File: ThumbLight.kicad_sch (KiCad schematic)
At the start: 4 parts, among them J1 USB_A, U2 UA78M33_TO252, U3 ESP-12E, U4 TTL

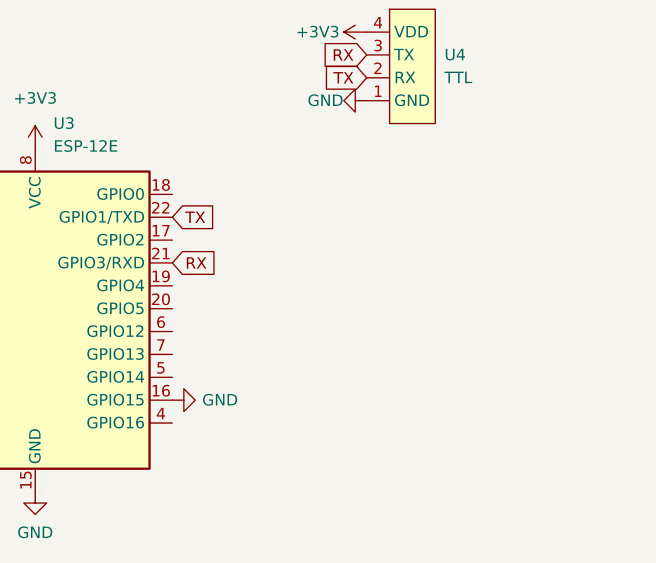
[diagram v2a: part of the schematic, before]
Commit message: Add PROGRAM Jumper as well as a DHT11 sensor
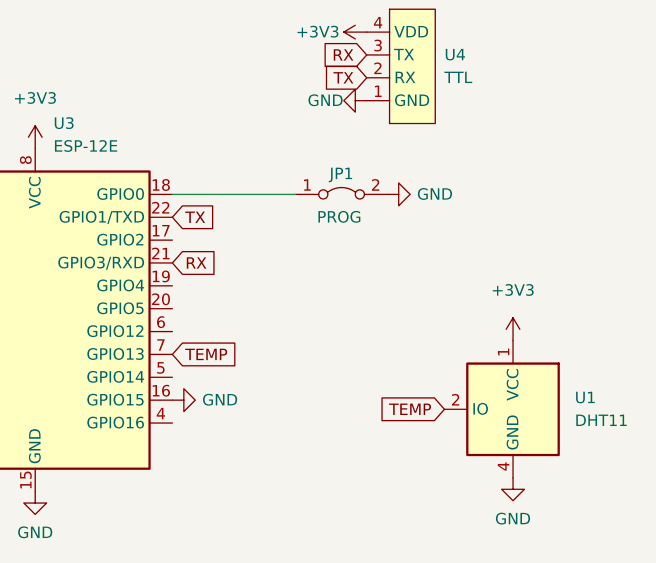
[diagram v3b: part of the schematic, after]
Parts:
- added JP1: PROG, Connector_PinHeader_2.54mm:PinHeader_1x02_P2.54mm_Vertical, symbol Jumper:Jumper_2_Bridged
- added U1: DHT11, Sensor:Aosong_DHT11_5.5x12.0_P2.54mm, symbol Sensor:DHT11
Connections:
- net +3V3: now also U1.1 (VCC)
- net GND: now also JP1.2 (B), U1.4 (GND)
- net at U3.18 (GPIO0): now also JP1.1 (A)
- net TEMP: now reaches U3.7 (GPIO13)
- net TEMP: now also U1.2 (IO)
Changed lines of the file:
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@@
   (no_connect (at 60.452 48.768))
   (no_connect (at 70.612 41.148))
+  (wire (pts (xy 141.224 48.514) (xy 154.94 48.514))
+    (stroke (width 0) (type default) (color 0 0 0 0))
+  )
   (global_label "TX" (shape input) (at 141.224 51.054 0) (fields_autoplaced)
     (effects (font (size 1.27 1.27)) (justify left))
@@
     )
   )
+  (global_label "TEMP" (shape input) (at 171.45 72.39 180) (fields_autoplaced)
+    (effects (font (size 1.27 1.27)) (justify right))
+    (property "Intersheet References" "${INTERSHEET_REFS}" (id 0) (at 164.1988 72.3106 0)
+      (effects (font (size 1.27 1.27)) (justify right) hide)
+    )
+  )
   (global_label "RX" (shape input) (at 141.224 56.134 0) (fields_autoplaced)
     (effects (font (size 1.27 1.27)) (justify left))
@@
     )
   )
+  (global_label "TEMP" (shape input) (at 141.224 66.294 0) (fields_autoplaced)
+    (effects (font (size 1.27 1.27)) (justify left))
+    (property "Intersheet References" "${INTERSHEET_REFS}" (id 0) (at 148.4752 66.3734 0)
+      (effects (font (size 1.27 1.27)) (justify left) hide)
+    )
+  )
+  (symbol (lib_id "power:+3V3") (at 179.07 64.77 0) (mirror y) (unit 1)
+    (in_bom yes) (on_board yes) (fields_autoplaced)
+    (property "Reference" "#PWR0114" (id 0) (at 179.07 68.58 0)
+      (effects (font (size 1.27 1.27)) hide)
+    )
+    (property "Value" "+3V3" (id 1) (at 179.07 59.182 0))
+    (property "Footprint" "" (id 2) (at 179.07 64.77 0)
+      (effects (font (size 1.27 1.27)) hide)
+    )
+    (property "Datasheet" "" (id 3) (at 179.07 64.77 0)
+      (effects (font (size 1.27 1.27)) hide)
+    )
+    (pin "1")
+  )
   (symbol (lib_id "power:GND") (at 141.224 71.374 90) (unit 1)
     (in_bom yes) (on_board yes) (fields_autoplaced)
@@
     )
     (pin "1")
+  )
+  (symbol (lib_id "Sensor:DHT11") (at 179.07 72.39 0) (mirror y) (unit 1)
+    (in_bom yes) (on_board yes) (fields_autoplaced)
+    (property "Reference" "U1" (id 0) (at 185.928 71.1199 0)
+      (effects (font (size 1.27 1.27)) (justify right))
+    )
+    (property "Value" "DHT11" (id 1) (at 185.928 73.6599 0)
+      (effects (font (size 1.27 1.27)) (justify right))
+    )
+    (property "Footprint" "Sensor:Aosong_DHT11_5.5x12.0_P2.54mm" (id 2) (at 179.07 82.55 0)
+      (effects (font (size 1.27 1.27)) hide)
+    )
+    (property "Datasheet" "http://akizukidenshi.com/download/ds/aosong/DHT11.pdf" (id 3) (at 175.26 66.04 0)
+      (effects (font (size 1.27 1.27)) hide)
+    )
+    (pin "1")
+    (pin "2")
+    (pin "3")
+    (pin "4")
   )
   (symbol (lib_id "power:+3V3") (at 162.814 30.48 90) (unit 1)
@@
     (pin "9")
   )
+  (symbol (lib_id "Jumper:Jumper_2_Bridged") (at 160.02 48.514 0) (unit 1)
+    (in_bom yes) (on_board yes)
+    (property "Reference" "JP1" (id 0) (at 160.02 46.228 0))
+    (property "Value" "PROG" (id 1) (at 159.766 51.054 0))
+    (property "Footprint" "Connector_PinHeader_2.54mm:PinHeader_1x02_P2.54mm_Vertical" (id 2) (at 160.02 48.514 0)
+      (effects (font (size 1.27 1.27)) hide)
+    )
+    (property "Datasheet" "~" (id 3) (at 160.02 48.514 0)
+      (effects (font (size 1.27 1.27)) hide)
+    )
+    (pin "1")
+    (pin "2")
+  )
   (symbol (lib_id "power:+3V3") (at 110.744 53.594 90) (unit 1)
     (in_bom yes) (on_board yes)
@@
     )
     (property "Datasheet" "" (id 3) (at 162.814 38.1 0)
+      (effects (font (size 1.27 1.27)) hide)
+    )
+    (pin "1")
+  )
+  (symbol (lib_id "power:GND") (at 179.07 80.01 0) (mirror y) (unit 1)
+    (in_bom yes) (on_board yes) (fields_autoplaced)
+    (property "Reference" "#PWR0113" (id 0) (at 179.07 86.36 0)
+      (effects (font (size 1.27 1.27)) hide)
+    )
+    (property "Value" "GND" (id 1) (at 179.07 84.582 0))
+    (property "Footprint" "" (id 2) (at 179.07 80.01 0)
+      (effects (font (size 1.27 1.27)) hide)
+    )
+    (property "Datasheet" "" (id 3) (at 179.07 80.01 0)
+      (effects (font (size 1.27 1.27)) hide)
+    )
+    (pin "1")
+  )
+  (symbol (lib_id "power:GND") (at 165.1 48.514 90) (unit 1)
+    (in_bom yes) (on_board yes) (fields_autoplaced)
+    (property "Reference" "#PWR0112" (id 0) (at 171.45 48.514 0)
+      (effects (font (size 1.27 1.27)) hide)
+    )
+    (property "Value" "GND" (id 1) (at 168.402 48.5139 90)
+      (effects (font (size 1.27 1.27)) (justify right))
+    )
+    (property "Footprint" "" (id 2) (at 165.1 48.514 0)
+      (effects (font (size 1.27 1.27)) hide)
+    )
+    (property "Datasheet" "" (id 3) (at 165.1 48.514 0)
       (effects (font (size 1.27 1.27)) hide)
     )
@@
       (reference "#PWR0111") (unit 1) (value "GND") (footprint "")
     )
+    (path "/cecaeb11-c18e-436a-b913-ea98641a8577"
+      (reference "#PWR0112") (unit 1) (value "GND") (footprint "")
+    )
+    (path "/cd1319fe-9fb0-446c-90b1-41f07d211857"
+      (reference "#PWR0113") (unit 1) (value "GND") (footprint "")
+    )
+    (path "/1537578c-25a2-4583-94d3-02f62cf698e2"
+      (reference "#PWR0114") (unit 1) (value "+3V3") (footprint "")
+    )
     (path "/b11863f2-05f0-4c70-9612-53388c5c7348"
       (reference "J1") (unit 1) (value "USB_A") (footprint "Connector_USB:USB_A_CNCTech_1001-011-01101_Horizontal")
     )
+    (path "/8fe39038-0f26-46f1-8a00-7161b7c20514"
+      (reference "JP1") (unit 1) (value "PROG") (footprint "Connector_PinHeader_2.54mm:PinHeader_1x02_P2.54mm_Vertical")
+    )
+    (path "/48072e63-67ef-42f2-9dd9-98f22a40c240"
+      (reference "U1") (unit 1) (value "DHT11") (footprint "Sensor:Aosong_DHT11_5.5x12.0_P2.54mm")
+    )
     (path "/efad0331-27eb-4636-86a4-200955527a64"

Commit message: Add USB Footprint
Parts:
- J1: footprint Connector_USB:USB_A_CNCTech_1001-011-01101_Horizontal -> usb-a-pcb:usb-a-pcb
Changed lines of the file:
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@@
     (property "Reference" "J1" (id 0) (at 62.992 25.4 0))
     (property "Value" "USB_A" (id 1) (at 62.992 27.94 0))
-    (property "Footprint" "Connector_USB:USB_A_CNCTech_1001-011-01101_Horizontal" (id 2) (at 66.802 39.878 0)
+    (property "Footprint" "usb-a-pcb:usb-a-pcb" (id 2) (at 66.802 39.878 0)
       (effects (font (size 1.27 1.27)) hide)
     )
@@
     )
     (path "/b11863f2-05f0-4c70-9612-53388c5c7348"
-      (reference "J1") (unit 1) (value "USB_A") (footprint "Connector_USB:USB_A_CNCTech_1001-011-01101_Horizontal")
+      (reference "J1") (unit 1) (value "USB_A") (footprint "usb-a-pcb:usb-a-pcb")
     )
     (path "/8fe39038-0f26-46f1-8a00-7161b7c20514"

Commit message: New basic layout
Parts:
- JP1: footprint Connector_PinHeader_2.54mm:PinHeader_1x02_P2.54mm_Vertical -> Connector_PinHeader_2.54mm:PinHeader_1x03_P2.54mm_Vertical
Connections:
- net TEMP: now also U3.19 (GPIO4); no longer U3.7 (GPIO13)
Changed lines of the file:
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@@
     )
   )
-  (global_label "TEMP" (shape input) (at 141.224 66.294 0) (fields_autoplaced)
+  (global_label "TEMP" (shape input) (at 141.224 58.674 0) (fields_autoplaced)
     (effects (font (size 1.27 1.27)) (justify left))
-    (property "Intersheet References" "${INTERSHEET_REFS}" (id 0) (at 148.4752 66.3734 0)
+    (property "Intersheet References" "${INTERSHEET_REFS}" (id 0) (at 148.4752 58.7534 0)
       (effects (font (size 1.27 1.27)) (justify left) hide)
     )
@@
     (property "Reference" "JP1" (id 0) (at 160.02 46.228 0))
     (property "Value" "PROG" (id 1) (at 159.766 51.054 0))
-    (property "Footprint" "Connector_PinHeader_2.54mm:PinHeader_1x02_P2.54mm_Vertical" (id 2) (at 160.02 48.514 0)
+    (property "Footprint" "Connector_PinHeader_2.54mm:PinHeader_1x03_P2.54mm_Vertical" (id 2) (at 160.02 48.514 0)
       (effects (font (size 1.27 1.27)) hide)
     )
@@
     )
     (path "/8fe39038-0f26-46f1-8a00-7161b7c20514"
-      (reference "JP1") (unit 1) (value "PROG") (footprint "Connector_PinHeader_2.54mm:PinHeader_1x02_P2.54mm_Vertical")
+      (reference "JP1") (unit 1) (value "PROG") (footprint "Connector_PinHeader_2.54mm:PinHeader_1x03_P2.54mm_Vertical")
     )
     (path "/48072e63-67ef-42f2-9dd9-98f22a40c240"

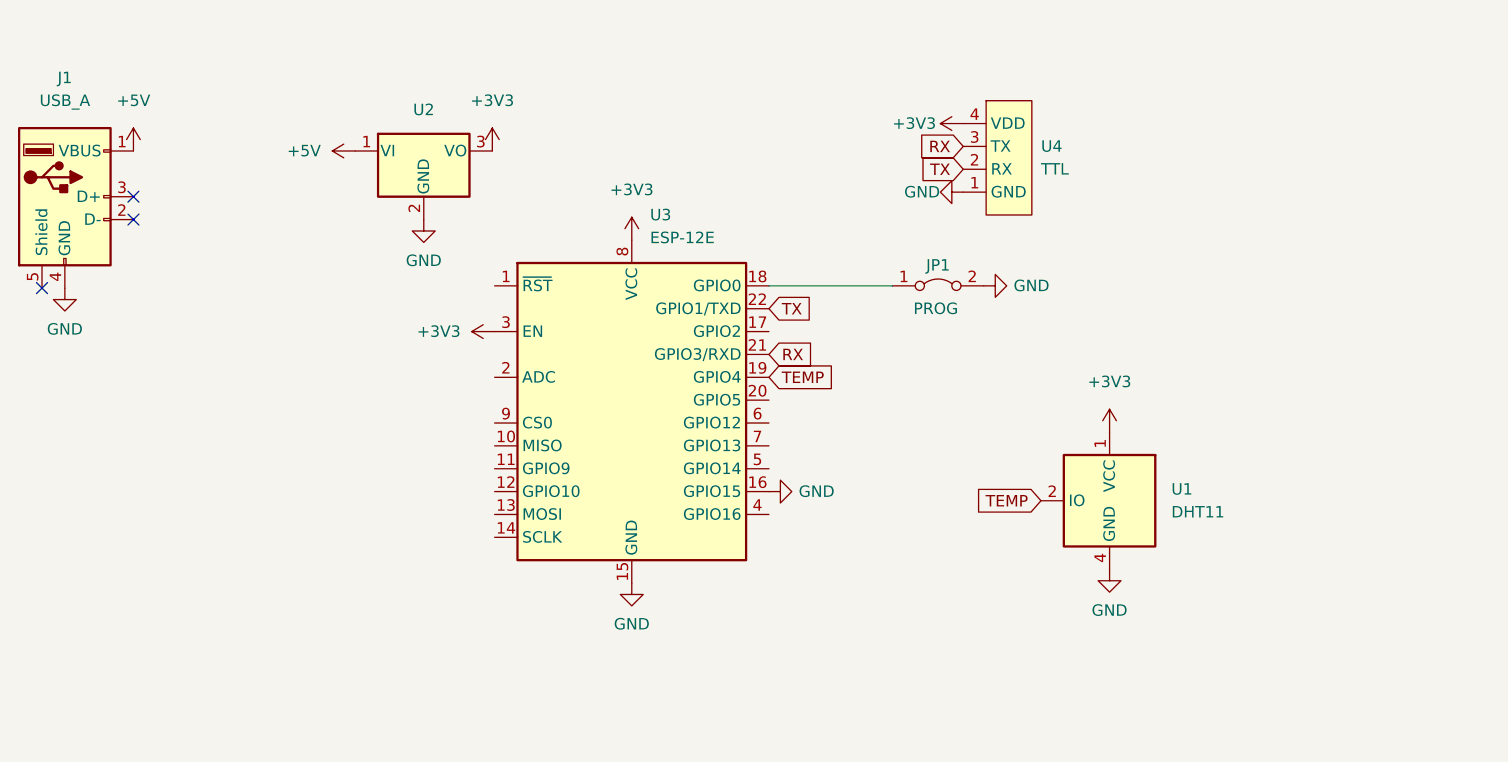
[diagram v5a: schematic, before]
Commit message: Add neopixel strip
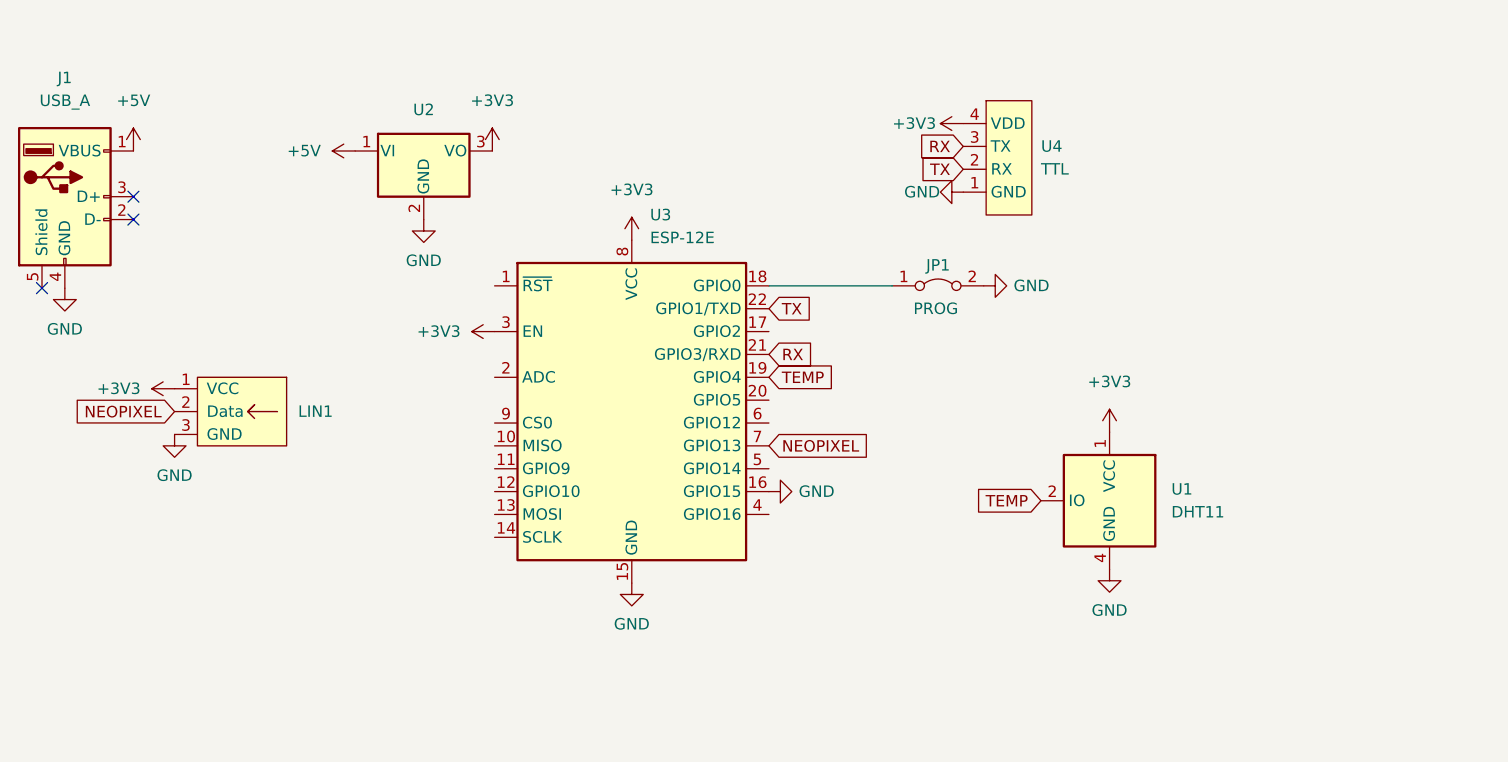
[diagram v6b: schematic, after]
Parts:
- added LIN1: LEDs_In, neopixel-strip:neopixel-strip, symbol neopixel-strip:LEDs_In
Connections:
- net +3V3: now also LIN1.1 (VCC)
- net GND: now also LIN1.3 (GND)
- net NEOPIXEL: now reaches U3.7 (GPIO13)
- net NEOPIXEL: now also LIN1.2 (Data)
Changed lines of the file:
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@@
     (stroke (width 0) (type default) (color 0 0 0 0))
+  )
+  (global_label "NEOPIXEL" (shape input) (at 141.224 66.294 0) (fields_autoplaced)
+    (effects (font (size 1.27 1.27)) (justify left))
+    (property "Intersheet References" "${INTERSHEET_REFS}" (id 0) (at 152.7085 66.2146 0)
+      (effects (font (size 1.27 1.27)) (justify left) hide)
+    )
   )
   (global_label "TX" (shape input) (at 141.224 51.054 0) (fields_autoplaced)
@@
     )
   )
+  (global_label "NEOPIXEL" (shape input) (at 75.184 62.484 180) (fields_autoplaced)
+    (effects (font (size 1.27 1.27)) (justify right))
+    (property "Intersheet References" "${INTERSHEET_REFS}" (id 0) (at 63.6995 62.5634 0)
+      (effects (font (size 1.27 1.27)) (justify right) hide)
+    )
+  )
   (symbol (lib_id "power:+3V3") (at 179.07 64.77 0) (mirror y) (unit 1)
     (in_bom yes) (on_board yes) (fields_autoplaced)
@@
     )
     (pin "1")
+  )
+  (symbol (lib_id "neopixel-strip:LEDs_In") (at 82.804 62.484 0) (mirror y) (unit 1)
+    (in_bom yes) (on_board yes) (fields_autoplaced)
+    (property "Reference" "LIN1" (id 0) (at 88.9 62.4839 0)
+      (effects (font (size 1.27 1.27)) (justify right))
+    )
+    (property "Value" "LEDs_In" (id 1) (at 82.804 67.564 0)
+      (effects (font (size 1.27 1.27)) hide)
+    )
+    (property "Footprint" "neopixel-strip:neopixel-strip" (id 2) (at 81.534 70.104 0)
+      (effects (font (size 1.27 1.27)) hide)
+    )
+    (property "Datasheet" "" (id 3) (at 84.582 54.864 0)
+      (effects (font (size 1.27 1.27)) hide)
+    )
+    (pin "1")
+    (pin "2")
+    (pin "3")
   )
   (symbol (lib_id "Sensor:DHT11") (at 179.07 72.39 0) (mirror y) (unit 1)
@@
     (pin "1")
   )
+  (symbol (lib_id "power:GND") (at 75.184 65.024 0) (unit 1)
+    (in_bom yes) (on_board yes) (fields_autoplaced)
+    (property "Reference" "#PWR0116" (id 0) (at 75.184 71.374 0)
+      (effects (font (size 1.27 1.27)) hide)
+    )
+    (property "Value" "GND" (id 1) (at 75.184 69.596 0))
+    (property "Footprint" "" (id 2) (at 75.184 65.024 0)
+      (effects (font (size 1.27 1.27)) hide)
+    )
+    (property "Datasheet" "" (id 3) (at 75.184 65.024 0)
+      (effects (font (size 1.27 1.27)) hide)
+    )
+    (pin "1")
+  )
   (symbol (lib_id "Connector:USB_A") (at 62.992 38.608 0) (unit 1)
     (in_bom yes) (on_board yes) (fields_autoplaced)
@@
     (pin "4")
   )
+  (symbol (lib_id "power:+3V3") (at 75.184 59.944 90) (unit 1)
+    (in_bom yes) (on_board yes)
+    (property "Reference" "#PWR0115" (id 0) (at 78.994 59.944 0)
+      (effects (font (size 1.27 1.27)) hide)
+    )
+    (property "Value" "+3V3" (id 1) (at 66.548 59.944 90)
+      (effects (font (size 1.27 1.27)) (justify right))
+    )
+    (property "Footprint" "" (id 2) (at 75.184 59.944 0)
+      (effects (font (size 1.27 1.27)) hide)
+    )
+    (property "Datasheet" "" (id 3) (at 75.184 59.944 0)
+      (effects (font (size 1.27 1.27)) hide)
+    )
+    (pin "1")
+  )
   (symbol (lib_id "Regulator_Linear:KA78M05_TO252") (at 102.87 33.528 0) (unit 1)
     (in_bom yes) (on_board yes)
@@
       (reference "#PWR0114") (unit 1) (value "+3V3") (footprint "")
     )
+    (path "/e146b4be-804d-4b5e-b688-037465072494"
+      (reference "#PWR0115") (unit 1) (value "+3V3") (footprint "")
+    )
+    (path "/a38d067c-e4c4-49b6-a584-c1e3a2dfc212"
+      (reference "#PWR0116") (unit 1) (value "GND") (footprint "")
+    )
     (path "/b11863f2-05f0-4c70-9612-53388c5c7348"
       (reference "J1") (unit 1) (value "USB_A") (footprint "usb-a-pcb:usb-a-pcb")
@@
       (reference "JP1") (unit 1) (value "PROG") (footprint "Connector_PinHeader_2.54mm:PinHeader_1x03_P2.54mm_Vertical")
     )
+    (path "/2f0d9e17-0017-4f0a-97f2-a84fa9e7a5e6"
+      (reference "LIN1") (unit 1) (value "LEDs_In") (footprint "neopixel-strip:neopixel-strip")
+    )
     (path "/48072e63-67ef-42f2-9dd9-98f22a40c240"

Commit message: Add buttons and light sensor
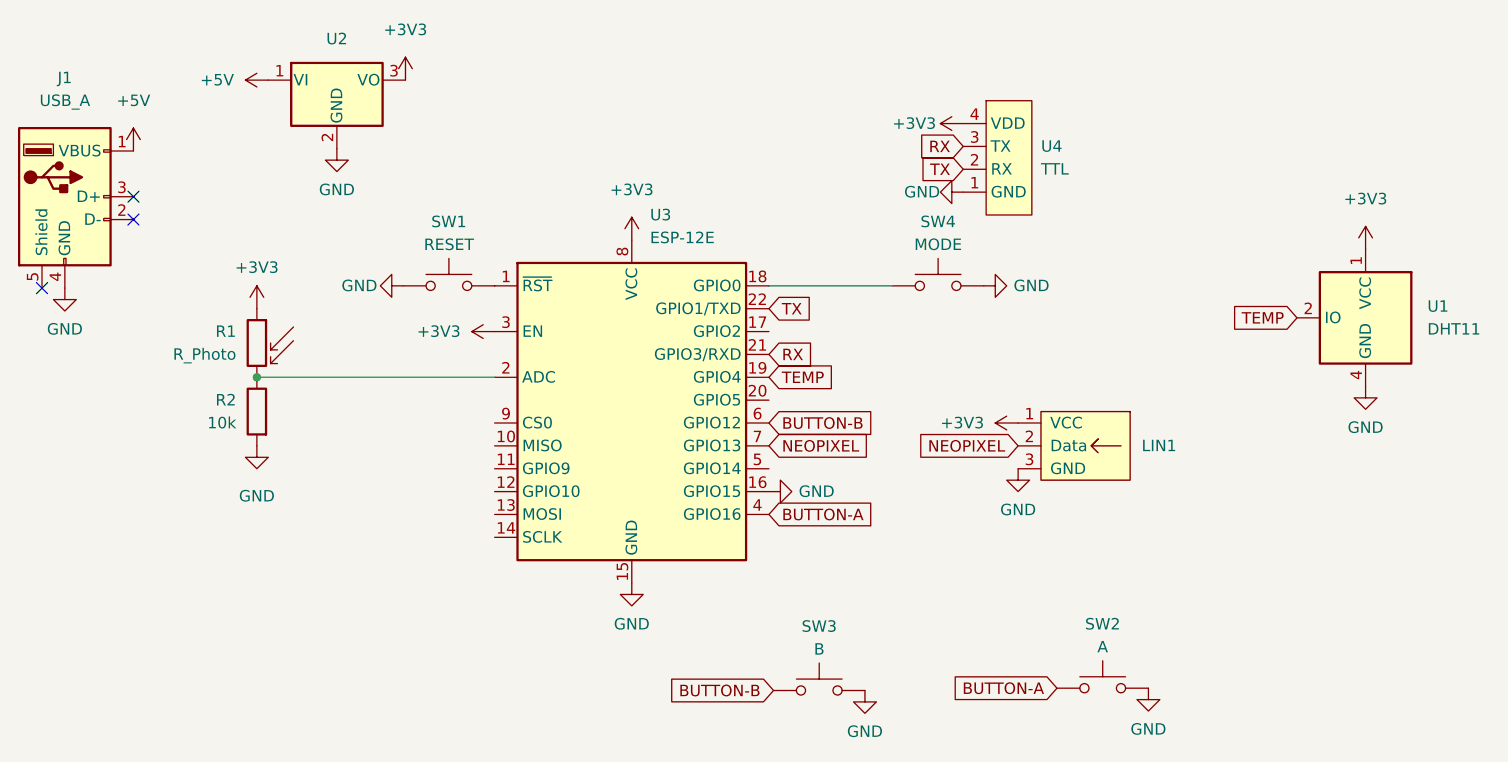
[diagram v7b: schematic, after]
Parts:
- removed JP1: PROG, Connector_PinHeader_2.54mm:PinHeader_1x03_P2.54mm_Vertical, symbol Jumper:Jumper_2_Bridged
- added R1: R_Photo, OptoDevice:R_LDR_5.0x4.1mm_P3mm_Vertical, symbol Device:R_Photo
- added R2: 10k, Resistor_THT:R_Axial_DIN0207_L6.3mm_D2.5mm_P7.62mm_Horizontal, symbol Device:R
- added SW1: RESET, Button_Switch_SMD:SW_Push_1P1T_NO_Vertical_Wuerth_434133025816, symbol Switch:SW_Push
- added SW2: A, Button_Switch_SMD:SW_Push_1P1T_NO_Vertical_Wuerth_434133025816, symbol Switch:SW_Push
- added SW3: B, Button_Switch_SMD:SW_Push_1P1T_NO_Vertical_Wuerth_434133025816, symbol Switch:SW_Push
- added SW4: MODE, Button_Switch_SMD:SW_Push_1P1T_NO_Vertical_Wuerth_434133025816, symbol Switch:SW_Push
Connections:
- net +3V3: now also R1.1
- net GND: now also R2.2, SW1.1, SW2.1, SW3.1, SW4.1
- net at U3.1 (~{RST}): now also SW1.2
- net at U3.18 (GPIO0): now also SW4.2
- net at U3.2 (ADC): now also R1.2, R2.1
- net BUTTON-A: now reaches U3.4 (GPIO16)
- net BUTTON-A: now also SW2.2
- net BUTTON-B: now reaches U3.6 (GPIO12)
- net BUTTON-B: now also SW3.2
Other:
- moved on the sheet: LIN1, U1, U2

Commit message: v1.1-beta improvements
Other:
- company: (none) -> Besmer Labs
- title: (none) -> ThumbLight
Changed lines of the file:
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@@
 (kicad_sch (version 20211123) (generator eeschema)
-  (paper "A4")
+  (paper "E")
+  (title_block
+    (title "ThumbLight")
+    (date "2023-11-28")
+    (rev "v1.1-beta")
+    (company "Besmer Labs")
+  )
   (junction (at 84.328 58.674) (diameter 0) (color 0 0 0 0)
   )
